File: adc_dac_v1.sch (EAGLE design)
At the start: 48 parts, among them IC1 LT6220, IC2 OPA353NA3K, IC3 ADA4001-2, IC4 AD8031RJ, U1 AD7960BCPZ-RL7, U2 AD5453YRMZ-REEL7, U3 ADA4932-1YCPZ-R7

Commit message: extensive schematic updates
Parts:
- removed IC2: OPA353NA3K, linear:MCP601SN
- removed IC4: AD8031RJ, analog-devices:AD8031RJ
- added C21: 1u, rcl:C-USC0603
- added C22, C23, C24, C25, C26, C27: 0.1u, rcl:C-USC0603
- added JP1: (no value), pinhead:PINHD-1X4
- added R21: 1k, rcl:R-US_R0603
- added R22: 2k, rcl:R-US_R0603
- added R23: DNP, rcl:R-US_R0603
- added R24: 0, rcl:R-US_R0603
- added U10: UA78M05CDCYR, open_covg:UA78M05CDCYR
- added U11: LP5907MFX-1.8/NOPB, open_covg:LP5907MFX-1.8/NOPB
- added U4, U5: NLSX3018DTR2G, open_covg:NLSX3018DTR2G
- added U6: ADS7952SRHBT, open_covg:ADS7952SRHBT
- added U7: Value, open_covg:OPA192IDBVR
- added U8: REF5025AIDR, open_covg:REF5025AIDR
- added U9: ADP150AUJZ-3.3-R7, open_covg:ADP150AUJZ-3.3-R7
- added X1, X2: BU-SMA-G, con-coax:BU-SMA-G
- C1: value 0.1u -> 1u
- C11, C14, C15, C16, C17, C18, C19, C20, C4, C5: device rcl:C-USC0805 -> rcl:C-USC0603
- C2: value 0.1u -> 2.2u
- IC1: value LT6220 -> OPA1662; device linear:MCP601SN -> open_covg:OPA1662
- IC3: value ADA4001-2 -> ADA4610-2
- R14, R6: value 0 -> 1k
- R18: value DNO -> DNP
- R2, R3: value 60k -> 20k
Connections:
- removed net +5V: C1.1, C11.1, C14.1, C15.1, C17.1, C4.1, C8.1, C9.1, IC1.V+, U1.VDD1, U1.VDD1_2, U1.VDD1_3
- removed net -5V: C2.1, C5.1, IC1.V-
- removed net 3V3_REF: IC2.+IN, U3.IN+
- removed net AGND: C1.2, C10.2, C2.2, C3.2, C4.2, C5.2, C6.2, C7.2, C8.2, C9.2, IC1.-IN, IC2.V-, IC3A.IN-, R4.1, R4.2, U1.!LDAC, U1.AGNDF, U1.AGNDS, U1.DGND, U1.EPAD, U2.GND, U3.V-
- removed net DAC_VAL: IC1.+IN, U1.VOUT
- removed net N$6: C1.1, IC2.OUT, R1.2, R12.1, R5.1, U1.VREF-F, U1.VREF-S, U2.OUT-, U3.IN-
- removed net REF_5V: IC1.IN+, IC4.IN+
- new net 2V5_REF: C2.1, U6.REFP, U8.VOUT
- new net 5V: C14.1, C15.1, C17.1, C22.1, C25.1, U1.VDD1, U1.VDD1_2, U1.VDD1_3, U6.VA+, U6.VA+_2, U7.V+
- new net 5V_REF: IC1A.IN+
- new net JP1-1: OK1JP1_ODD.+VDC_1
- new net JP1-10: OK1JP1_EVEN.USB_SCL
- new net JP1-11: OK1JP1_ODD.+3.3VDD_11
- new net JP1-12: OK1JP1_EVEN.USB_SDA
- new net JP1-13: OK1JP1_ODD.+3.3VDD_13
- new net JP1-14: OK1JP1_EVEN.DGND_14
- new net JP1-15: OK1JP1_ODD.W20-L60P_1
- new net JP1-16: OK1JP1_EVEN.T19-L74P_1
- new net JP1-17: OK1JP1_ODD.W22-L60N_1
- new net JP1-18: OK1JP1_EVEN.T20-L74N_1
- new net JP1-19: OK1JP1_ODD.U19-L70P_1
- new net JP1-2: OK1JP1_EVEN.DGND_2
- new net JP1-20: OK1JP1_EVEN.P17-L72P_1
- new net JP1-21: OK1JP1_ODD.V20-L70N_1
- new net JP1-22: OK1JP1_EVEN.N16-L72N_1
- new net JP1-23: OK1JP1_ODD.C5-L2P_0
- new net JP1-24: OK1JP1_EVEN.M17-L71P_1
- new net JP1-25: OK1JP1_ODD.A5-L2N_0
- new net JP1-26: OK1JP1_EVEN.M18-L71N_1
- new net JP1-27: OK1JP1_ODD.D14-L49P_0
- new net JP1-28: OK1JP1_EVEN.P18-L73P_1
- new net JP1-29: OK1JP1_ODD.C14-L49N_0
- new net JP1-3: OK1JP1_ODD.+VDC_3
- new net JP1-30: OK1JP1_EVEN.R19-L73N_1
- new net JP1-31: OK1JP1_ODD.E16-L66P_0
- new net JP1-32: OK1JP1_EVEN.D9-L7P_0
- new net JP1-33: OK1JP1_ODD.D17-L66N_0
- new net JP1-34: OK1JP1_EVEN.C8-L7N_0
- new net JP1-35: OK1JP1_ODD.DGND_35
- new net JP1-36: OK1JP1_EVEN.+VCCO0_36
- new net JP1-37: OK1JP1_ODD.D7-L32P_0
- new net JP1-38: OK1JP1_EVEN.D10-L33P_0
- new net JP1-39: OK1JP1_ODD.D8-L32N_0
- new net JP1-4: OK1JP1_EVEN.+1.2VDD_4
- new net JP1-40: OK1JP1_EVEN.C10-L33N_0
- new net JP1-41: OK1JP1_ODD.L17-L61P_1
- new net JP1-42: OK1JP1_EVEN.D11-L36P_0
- new net JP1-43: OK1JP1_ODD.K18-L61N_1
- new net JP1-44: OK1JP1_EVEN.C12-L36N_0
- new net JP1-45: OK1JP1_ODD.D6-L3P_0
- new net JP1-46: OK1JP1_EVEN.D15-L62P_0
- new net JP1-47: OK1JP1_ODD.C6-L3N_0
- new net JP1-48: OK1JP1_EVEN.C16-L62N_0
- new net JP1-49: OK1JP1_ODD.A3-L1P_0
- new net JP1-5: OK1JP1_ODD.+VDC_5
- new net JP1-50: OK1JP1_EVEN.B6-L4P_0
- new net JP1-51: OK1JP1_ODD.A4-L1N_0
- new net JP1-52: OK1JP1_EVEN.A6-L4N_0
- new net JP1-53: OK1JP1_ODD.B8-L6P_0
- new net JP1-54: OK1JP1_EVEN.C7-L5P_0
- new net JP1-55: OK1JP1_ODD.DGND_55
- new net JP1-56: OK1JP1_EVEN.+VCCO0_56
- new net JP1-57: OK1JP1_ODD.A8-L6N_0
- new net JP1-58: OK1JP1_EVEN.A7-L5N_0
- new net JP1-59: OK1JP1_ODD.B10-L34P_0
- new net JP1-6: OK1JP1_EVEN.+1.2VDD_6
- new net JP1-60: OK1JP1_EVEN.C9-L8P_0
- new net JP1-61: OK1JP1_ODD.A10-L34N_0
- new net JP1-62: OK1JP1_EVEN.A9-L8N_0
- new net JP1-63: OK1JP1_ODD.C13-L38P_0
- new net JP1-64: OK1JP1_EVEN.B12-L37P_0
- new net JP1-65: OK1JP1_ODD.A13-L38N_0
- new net JP1-66: OK1JP1_EVEN.A12-L37N_0
- new net JP1-67: OK1JP1_ODD.C15-L51P_0
- new net JP1-68: OK1JP1_EVEN.B14-L50P_0
- new net JP1-69: OK1JP1_ODD.A15-L51N_0
- new net JP1-7: OK1JP1_ODD.+1.8VDD
- new net JP1-70: OK1JP1_EVEN.A14-L50N_0
- new net JP1-71: OK1JP1_ODD.C17-L64P_0
- new net JP1-72: OK1JP1_EVEN.B16-L63P_0
- new net JP1-73: OK1JP1_ODD.A17-L64N_0
- new net JP1-74: OK1JP1_EVEN.A16-L63N_0
- new net JP1-75: OK1JP1_ODD.A18-L65N_0
- new net JP1-76: OK1JP1_EVEN.B18-L65P_0
- new net JP1-77: OK1JP1_ODD.C11-L35P_0
- new net JP1-78: OK1JP1_EVEN.DGND_78
- new net JP1-79: OK1JP1_ODD.A11-L35N_0
- new net JP1-8: OK1JP1_EVEN.SYS_CLK5
- new net JP1-80: OK1JP1_EVEN.DGND_80
- new net JP1-9: OK1JP1_ODD.+3.3VDD_9
- new net JP2-1: OK1JP2_ODD.DGND_1
- new net JP2-10: OK1JP2_EVEN.VREF_1
- new net JP2-11: OK1JP2_ODD.SYS_CLK4
- new net JP2-12: OK1JP2_EVEN.NC_12
- new net JP2-13: OK1JP2_ODD.DGND_13
- new net JP2-14: OK1JP2_EVEN.DGND_14
- new net JP2-15: OK1JP2_ODD.G16-L9P_1
- new net JP2-16: OK1JP2_EVEN.G19-L33P_1
- new net JP2-17: OK1JP2_ODD.G17-L9N_1
- new net JP2-18: OK1JP2_EVEN.F20-L33N_1
- new net JP2-19: OK1JP2_ODD.H19-L34P_1
- new net JP2-2: OK1JP2_EVEN.+3.3VDD_2
- new net JP2-20: OK1JP2_EVEN.H20-L38P_1
- new net JP2-21: OK1JP2_ODD.H18-L34N_1
- new net JP2-22: OK1JP2_EVEN.J19-L38N_1
- new net JP2-23: OK1JP2_ODD.F16-L10P_1
- new net JP2-24: OK1JP2_EVEN.D19-L29P_1
- new net JP2-25: OK1JP2_ODD.F17-L10N_1
- new net JP2-26: OK1JP2_EVEN.D20-L29N_1
- new net JP2-27: OK1JP2_ODD.J17-L36P_1
- new net JP2-28: OK1JP2_EVEN.F18-L30P_1
- new net JP2-29: OK1JP2_ODD.K17-L36N_1
- new net JP2-3: OK1JP2_ODD.NC_3
- new net JP2-30: OK1JP2_EVEN.F19-L30N_1
- new net JP2-31: OK1JP2_ODD.K16-L21P_1
- new net JP2-32: OK1JP2_EVEN.M16-L58P_1
- new net JP2-33: OK1JP2_ODD.J16-L21N_1
- new net JP2-34: OK1JP2_EVEN.L15-L58N_1
- new net JP2-35: OK1JP2_ODD.+VCCO1_35
- new net JP2-36: OK1JP2_EVEN.DGND_36
- new net JP2-37: OK1JP2_ODD.V21-L52P_1
- new net JP2-38: OK1JP2_EVEN.K20-L40P_1
- new net JP2-39: OK1JP2_ODD.V22-L52N_1
- new net JP2-4: OK1JP2_EVEN.+3.3VDD_4
- new net JP2-40: OK1JP2_EVEN.K19-L40N_1
- new net JP2-41: OK1JP2_ODD.T21-L50P_1
- new net JP2-42: OK1JP2_EVEN.U20-L51P_1
- new net JP2-43: OK1JP2_ODD.T22-L50N_1
- new net JP2-44: OK1JP2_EVEN.U22-L51N_1
- new net JP2-45: OK1JP2_ODD.P21-L48P_1
- new net JP2-46: OK1JP2_EVEN.R20-L49P_1
- new net JP2-47: OK1JP2_ODD.P22-L48N_1
- new net JP2-48: OK1JP2_EVEN.R22-L49N_1
- new net JP2-49: OK1JP2_ODD.M21-L46P_1
- new net JP2-5: OK1JP2_ODD.JTAG_TCK
- new net JP2-50: OK1JP2_EVEN.N20-L47P_1
- new net JP2-51: OK1JP2_ODD.M22-L46N_1
- new net JP2-52: OK1JP2_EVEN.N22-L47N_1
- new net JP2-53: OK1JP2_ODD.L20-L45P_1
- new net JP2-54: OK1JP2_EVEN.M20-L42P_1
- new net JP2-55: OK1JP2_ODD.+VCCO1_55
- new net JP2-56: OK1JP2_EVEN.DGND_56
- new net JP2-57: OK1JP2_ODD.L22-L45N_1
- new net JP2-58: OK1JP2_EVEN.L19-L42N_1
- new net JP2-59: OK1JP2_ODD.H21-L41P_1
- new net JP2-6: OK1JP2_EVEN.+3.3VDD_6
- new net JP2-60: OK1JP2_EVEN.K21-L44P_1
- new net JP2-61: OK1JP2_ODD.H22-L41N_1
- new net JP2-62: OK1JP2_EVEN.K22-L44N_1
- new net JP2-63: OK1JP2_ODD.F21-L37P_1
- new net JP2-64: OK1JP2_EVEN.G20-L39P_1
- new net JP2-65: OK1JP2_ODD.F22-L37N_1
- new net JP2-66: OK1JP2_EVEN.G22-L39N_1
- new net JP2-67: OK1JP2_ODD.D21-L31P_1
- new net JP2-68: OK1JP2_EVEN.E20-L35P_1
- new net JP2-69: OK1JP2_ODD.D22-L31N_1
- new net JP2-7: OK1JP2_ODD.JTAG_TMS
- new net JP2-70: OK1JP2_EVEN.E22-L35N_1
- new net JP2-71: OK1JP2_ODD.B21-L19P_1
- new net JP2-72: OK1JP2_EVEN.C20-L32P_1
- new net JP2-73: OK1JP2_ODD.B22-L19N-1
- new net JP2-74: OK1JP2_EVEN.C22-L32N_1
- new net JP2-75: OK1JP2_ODD.A21-L20N_1
- new net JP2-76: OK1JP2_EVEN.A20-L20P_1
- new net JP2-77: OK1JP2_ODD.J20-L43P_1
- new net JP2-78: OK1JP2_EVEN.DGND_78
- new net JP2-79: OK1JP2_ODD.J22-L43N_1
- new net JP2-8: OK1JP2_EVEN.JTAG_TDO
- new net JP2-80: OK1JP2_EVEN.DGND_80
- new net JP2-9: OK1JP2_ODD.JTAG_TDI
- new net N$19: U6.MXO, U7.IN+
- new net N$20: R23.1, R24.2, U7.IN-
- new net N$21: R24.1, U6.AINP, U7.OUT
- new net N$22: C21.1, U8.VIN
- new net N$23: U6.CH4
- new net N$24: C1.1, U8.TRIM/NR
- new net N$25: IC1A.OUT, R5.1, R6.2
- new net TR: U6.CH0, U8.TEMP
- net +15V: now also C24.1, IC1P.V+
- net -15V: now also C23.1, IC1P.V-
- net 1.8V: now also C27.1; no longer C10.1, C3.1
- net 3V3: now also C26.1, U6.VBD+; no longer C2.1, U1.VDD, U3.V+
- net AMP_PWR+: no longer C1.1, IC1.+VS, IC4.+VS, U2.PD, U2.VS+, U2.VS+_2, U2.VS+_3, U2.VS+_4
- net AMP_PWR-: now also C18.2; no longer U2.VS-, U2.VS-_2, U2.VS-_3, U2.VS-_4
- net CLK+: no longer R2.1
- net CLK-: no longer R2.2
- net CNV+: no longer R10.2
- net CNV-: no longer R10.1
- net CSB: no longer U1.!CS
- net DIFF_IN+: now also JP1.1, X1.1; no longer R4.1
- net DIFF_IN-: now also JP1.4, X2.1; no longer R5.1
- net GND: now also C21.2, C22.2, C23.2, C24.2, C25.2, C26.2, C27.2, IC1B.IN-, IC3A.IN-, JP1.2, JP1.3, R14.1, R22.2, R23.2, U2.GND, U6.AGND, U6.AGND_2, U6.AINM, U6.BDGND, U6.CH12, U6.CH13, U6.CH14, U6.CH15, U6.REFM, U7.V-, U8.GND, X1.2, X2.2; no longer C18.2, C3.2, IC1.-VS, IC4.-VS, R11.2, R3.1, U2.EPAD
- net IN+: no longer R13.2
- net IN-: no longer R12.2
- net N$1: now also IC1B.IN+; no longer IC1.+IN, IC1.IN-, IC1.OUT, R1.1
- net N$10: now also IC3B.IN-, R21.2, R22.1; no longer IC4.IN-, IC4.OUT, R14.1
- net N$11: no longer R6.1, R8.2, U2.IN+
- net N$12: no longer R6.2, U2.FB-
- net N$13: no longer R7.1, R9.2, U2.IN-
- net N$14: no longer R7.2, U2.FB+
- net N$2: no longer C12.1, IC1.-IN, IC1.OUT, R11.1, R2.2, R3.1, R4.2, R8.1, U1.INV
- net N$3: no longer C2.1, R5.2, R9.1, U1.RFB
- net N$4: now also IC1B.OUT; no longer IC1.OUT, U1.VDD2_3, U3.OUT
- net N$5: now also IC3B.IN+; no longer R13.1, R7.1, U2.OUT+
- net N$7: now also IC1A.IN-, R14.2, R6.1; no longer R3.1, U2.VREF
- net N$8: now also IC3B.OUT, R21.1, R7.1; no longer IC2.V+
- net OUT: no longer C3.1, R3.2
- net REF: no longer C6.1, C7.1, R1.2, R14.2
- net SCLK: no longer U1.SCLK
- net SDI: no longer U1.SDI
- net VCM: no longer U2.VOCM
- net VREF_BUF: now also R3.1, U2.VREF; no longer IC2.-IN
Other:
- note added: "16.7 MHz GBW"
- note added: "Need +2.048V ref here"
- note added: "Use internal buffer with 2.048V ref. EN3=X, EN2=0, EN1=0, EN0=1 (28 MHz BW) EN3=X, EN2=1, EN1=0, EN0=1 (9 MHz BW)"
- note added: "VA+ analog supply. 5V allows Range 2: VREF*2 VBD+ is digital I/O supply"
- note added: "VDD should match level of SPI interface 110 ns settling time"
- note added: "VDD2 and VIO can come from the same supply. But route and decouple separately."
- note added: "VREF buffer 9 kOhm VREF input resistance Gain to 10 V (AD5443 max is 12 V)"
- note added: "amp allows for: +3 to +/-5V supply output swing: 1.4 V of rails Eval Brd uses +7V and -2.5V"
- note removed: "+3 to +/-5V supply output swing: 1.4 V of rails Eval Brd uses +7V and -2.5V"
- note removed: "Need buffered +5V here"
- note removed: "Use externally buffered reference of 5V. EN3=X, EN2=1, EN1=0, EN0=1"
- note removed: "VDD should match level of SPI interface VREF VR02"
- note removed: "VREF <= VDD VDD from 2.7 to 5.5V VDD should match level of SPI interface"
- note removed: "VREF buffer"

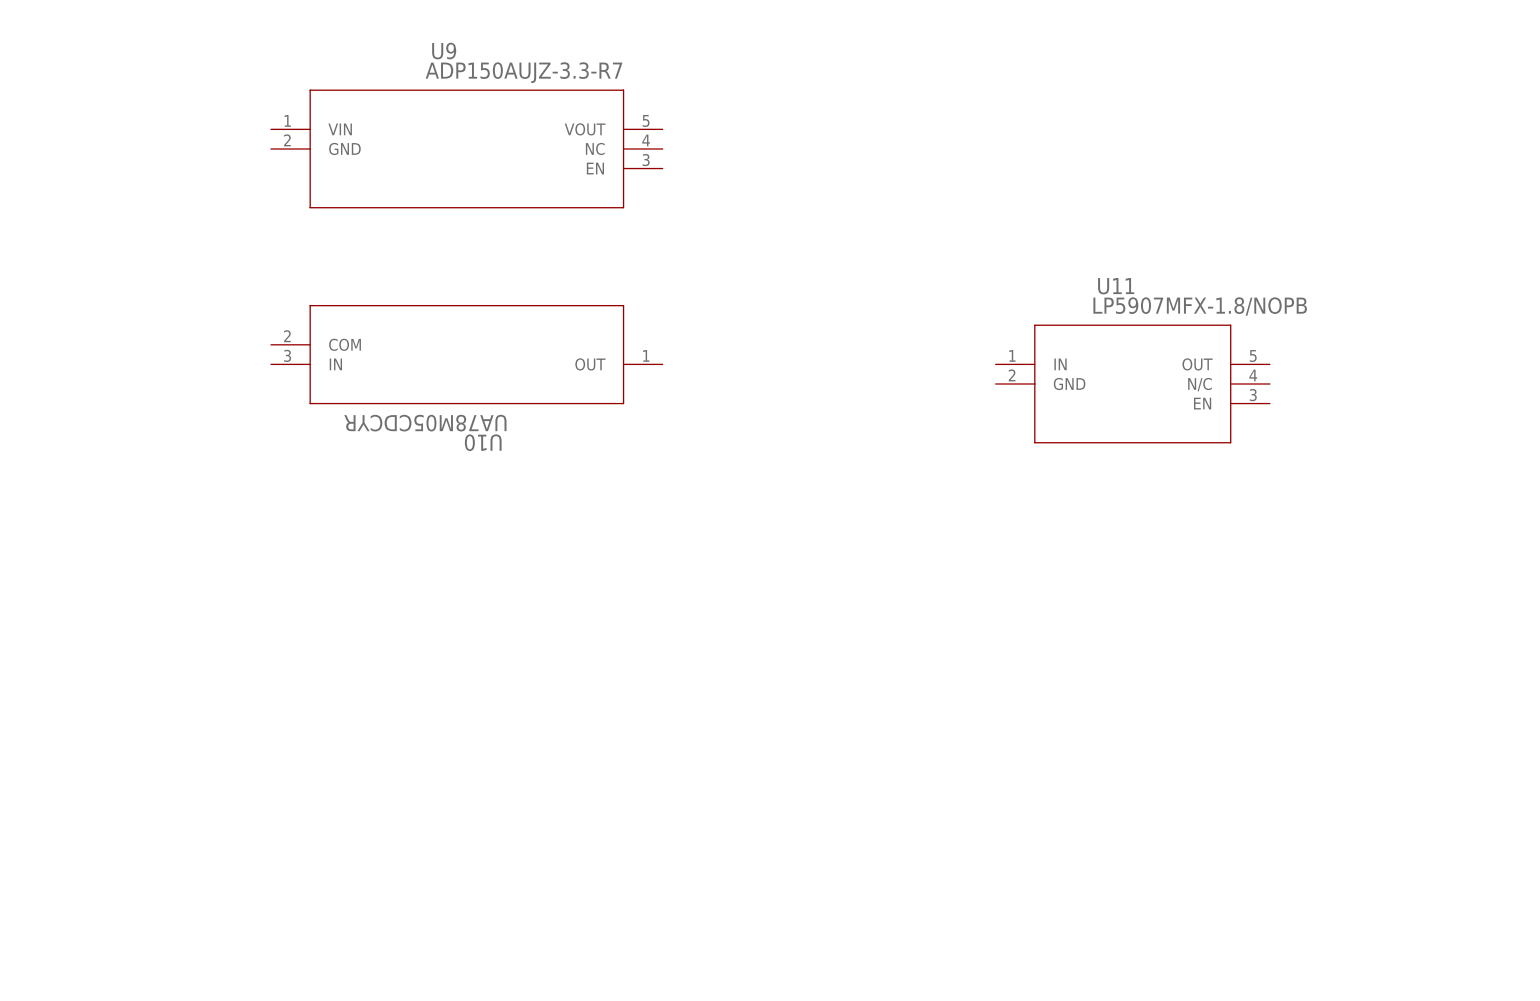
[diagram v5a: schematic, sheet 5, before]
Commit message: updated power supplies
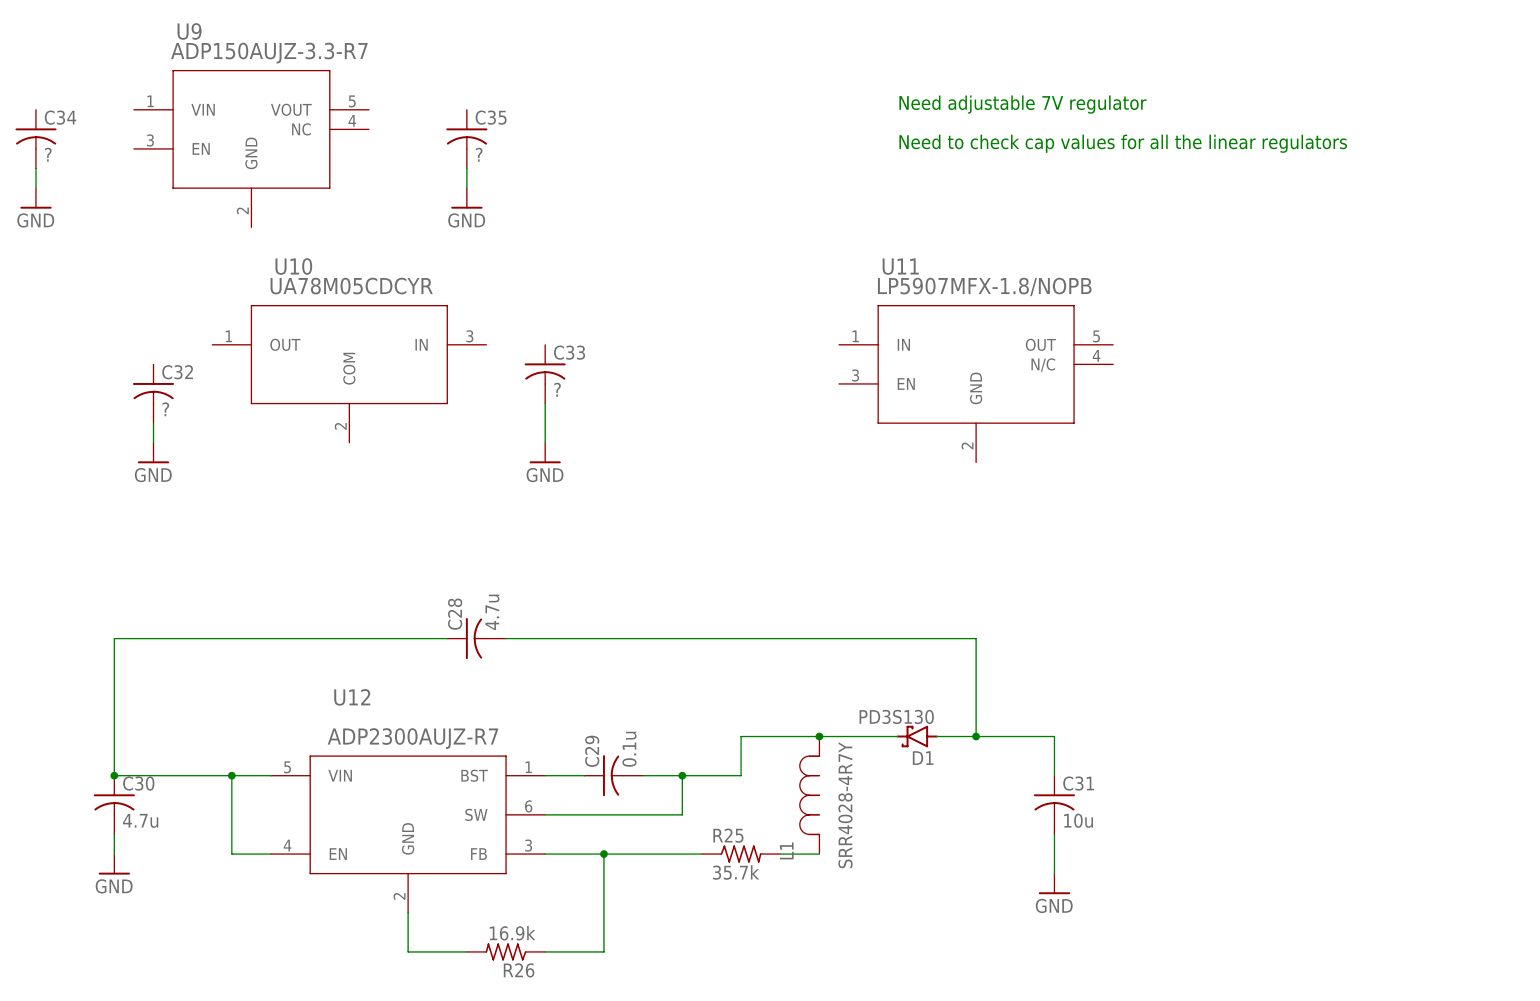
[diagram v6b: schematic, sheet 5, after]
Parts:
- added C28, C30: 4.7u, rcl:C-USC0603
- added C29: 0.1u, rcl:C-USC0603
- added C31: 10u, rcl:C-USC0603
- added C32, C33, C34, C35: ?, rcl:C-USC0603
- added D1: PD3S130, diode:PD3S160
- added L1: SRR4028-4R7Y, open_covg:SRR4028-4R7Y
- added R25: 35.7k, rcl:R-US_R0603
- added R26: 16.9k, rcl:R-US_R0603
- added U12: ADP2300AUJZ-R7, open_covg:ADP2300AUJZ-R7
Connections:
- new net 5V1: C28.1, C30.1, U12.EN, U12.VIN
- new net GND1: C28.2, C31.1, D1.A
- new net N$26: R25.1, R26.1, U12.FB
- new net N$27: C29.1, U12.BST
- new net N$29: C29.2, D1.C, L1.1, U12.SW
- new net N$30: R26.2, U12.GND
- new net N$6: L1.2, R25.2
- net GND: now also C30.2, C31.2, C32.2, C33.2, C34.2, C35.2
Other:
- note added: "Need adjustable 7V regulator"
- note added: "Need to check cap values for all the linear regulators"
- moved on the sheet: U10, U11, U9

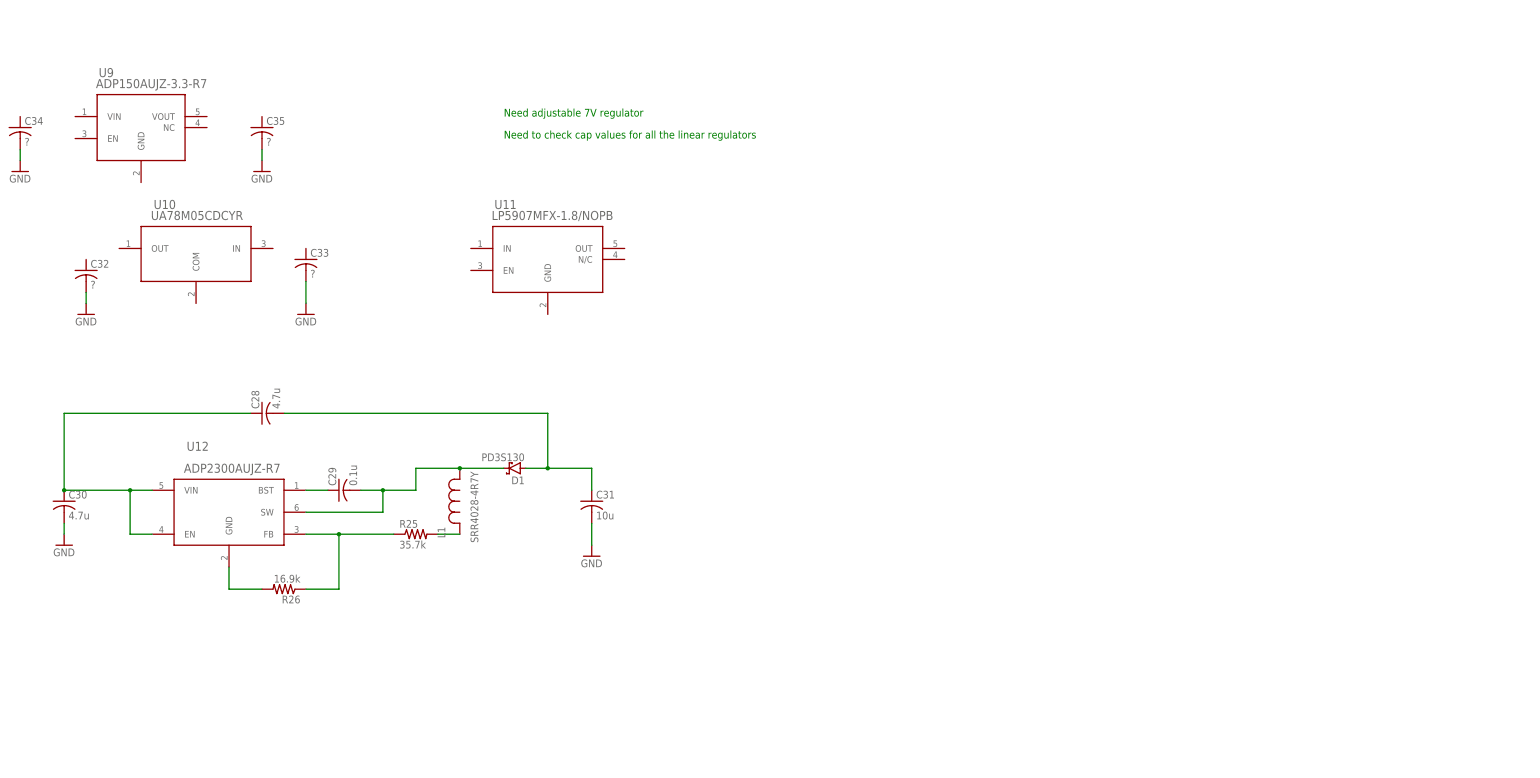
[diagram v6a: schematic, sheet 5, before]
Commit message: finished power supplies
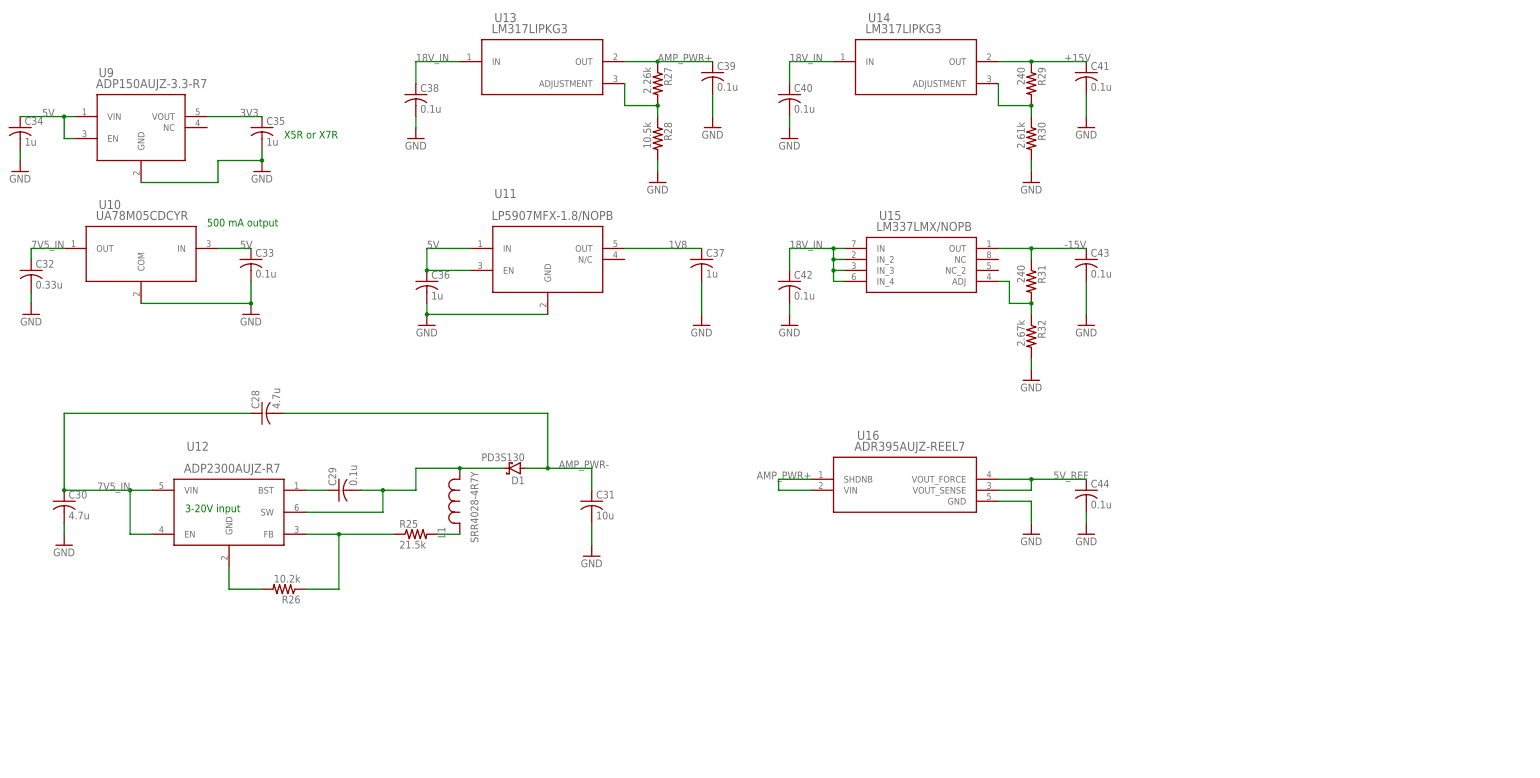
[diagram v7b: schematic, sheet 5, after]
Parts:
- added C36, C37: 1u, rcl:C-USC0603
- added C38, C39, C40, C41, C42, C43, C44: 0.1u, rcl:C-USC0603
- added R27: 2.26k, rcl:R-US_R0603
- added R28: 10.5k, rcl:R-US_R0603
- added R29, R31: 240, rcl:R-US_R0603
- added R30: 2.61k, rcl:R-US_R0603
- added R32: 2.67k, rcl:R-US_R0603
- added U13, U14: LM317LIPKG3, open_covg:LM317LIPKG3
- added U15: LM337LMX/NOPB, open_covg:LM337LMX/NOPB
- added U16: ADR395AUJZ-REEL7, open_covg:ADR395AUJZ-REEL7
- C32: value ? -> 0.33u
- C33: value ? -> 0.1u
- C34, C35: value ? -> 1u
- R25: value 35.7k -> 21.5k
- R26: value 16.9k -> 10.2k
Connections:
- removed net 1.8V: C11.1, C16.1, C27.1, U1.VDD2, U1.VDD2_2, U1.VIO
- removed net 5V1: C28.1, C30.1, U12.EN, U12.VIN
- removed net GND1: C28.2, C31.1, D1.A
- new net 18V_IN: C38.1, C40.1, C42.1, U13.IN, U14.IN, U15.IN, U15.IN_2, U15.IN_3, U15.IN_4
- new net 1V8: C11.1, C16.1, C27.1, C37.1, U1.VDD2, U1.VDD2_2, U1.VDD2_3, U1.VIO, U11.OUT
- new net 7V5_IN: C28.1, C30.1, C32.1, U10.OUT, U12.EN, U12.VIN
- new net N$28: R29.2, R30.1, U14.ADJUSTMENT
- new net N$32: R31.2, R32.1, U15.ADJ
- net +15V: now also C41.1, R29.1, U14.OUT
- net -15V: now also C43.1, R31.1, U15.OUT
- net 3V3: now also C35.1, U9.VOUT
- net 5V: now also C33.1, C34.1, C36.1, U10.IN, U11.EN, U11.IN, U9.EN, U9.VIN
- net 5V_REF: now also C44.1, U16.VOUT_FORCE, U16.VOUT_SENSE
- net AMP_PWR+: now also C39.1, R27.1, U13.OUT, U16.SHDNB, U16.VIN
- net AMP_PWR-: now also C28.2, C31.1, D1.A
- net GND: now also C36.2, C37.2, C38.2, C39.2, C40.2, C41.2, C42.2, C43.2, C44.2, R28.2, R30.2, R32.2, U10.COM, U11.GND, U16.GND, U9.GND
- net N$9: now also R27.2, R28.1, U13.ADJUSTMENT; no longer U1.VDD2_3
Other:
- note added: "3-20V input"
- note added: "500 mA output"
- note added: "X5R or X7R"
- note removed: "Need adjustable 7V regulator"
- note removed: "Need to check cap values for all the linear regulators"
- moved on the sheet: C32, C33, U10
